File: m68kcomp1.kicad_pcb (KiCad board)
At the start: 2 copper layers, 46 parts, among them P1 CONN_CTL_DATA, P2 CONN_ADDR, P3 POWER, SW1 RST_SW, SW2 PWR_SW, U1 74LS04, U10 sram_um61512ak, U11 sram_um61512ak, U12 68010D, U13 at28c64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

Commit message: laying out the board
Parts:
- U13, U9: footprint Housings_DIP:DIP-28_W15.24mm -> m68kcomp1:DIP-28_W15.24mm_oval
- moved U12 94.0 mm to (160.0, 57.1), turned to 270 degrees
- moved U13 71.9 mm to (101.6, 101.6)
- moved U9 69.4 mm to (81.3, 101.6)
- moved U5 20.3 mm to (91.4, 25.4), turned to 270 degrees
- moved U15 15.2 mm to (160.0, 116.8)
- moved U16 15.2 mm to (176.5, 116.8)
- moved U10 15.2 mm to (127.0, 116.8)
- moved P1 15.2 mm to (199.4, 139.7)
- moved U11 15.2 mm to (143.5, 116.8)
- moved P2 9.67 mm to (196.8, 52.1)
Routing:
- net /D6: track 100.9 -> 154.1 mm
- net /D5: track 96.3 -> 146.4 mm
- net /D4: track 96.6 -> 143.3 mm
- net /D1: track 126.2 -> 171.4 mm
- net /D2: track 125.4 -> 169.8 mm
- net /D0: track 136.6 -> 178.8 mm
- net /D3: track 91.3 -> 130.6 mm
- net /A1: track 77.9 -> 96.7 mm
- net /A3: track 77.9 -> 96.6 mm
- net /A8: track 77.9 -> 96.6 mm
- net /A7: track 77.9 -> 96.6 mm
- net /A6: track 77.9 -> 96.6 mm
- net /A5: track 77.9 -> 96.6 mm
- net /A4: track 77.9 -> 96.6 mm
- net /A13: track 77.9 -> 96.6 mm
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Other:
- board outline added: 160 x 100 mm

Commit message: laying out the board
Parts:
- P2: footprint Pin_Headers:Pin_Header_Straight_2x13 -> m68kcomp1:Pin_Header_Straight_2x13_oval
- moved Y1 216.2 mm to (153.3, 48.8), turned to 180 degrees
- moved U6 205.6 mm to (154.4, 56.0), turned to 270 degrees
- moved U14 197.3 mm to (186.1, 47.0), turned to 270 degrees
- moved SW1 194.1 mm to (165.1, 47.6)
- moved D1 173.5 mm to (61.0, 49.0), turned to 270 degrees
- moved U7 168.2 mm to (135.2, 53.7)
- moved R8 149.6 mm to (57.0, 48.0), turned to 180 degrees
- moved SW2 121.9 mm to (57.0, 53.3), turned to 270 degrees
- moved U5 115.0 mm to (64.3, 137.2), turned to 0 degrees
- moved P3 47.6 mm to (52.0, 53.3)
- moved U12 21.3 mm to (180.3, 63.5)
- moved P2 3.81 mm to (196.8, 55.9)
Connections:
- P2 pad 1: GND -> /A1
- P2 pad 2: /A1 -> GND
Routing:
- net /A4: track 96.6 -> 204.1 mm
- net /A6: track 96.6 -> 203.1 mm
- net /A5: track 96.6 -> 203.1 mm
- net /~WR: track 52.7 -> 158.1 mm, vias 0 -> 1
- net /A2: track 96.5 -> 198.9 mm
- net /A3: track 96.6 -> 198.4 mm
- net /A7: track 96.6 -> 197.0 mm
- net /A8: track 96.6 -> 197.0 mm
- net /A1: track 96.7 -> 193.4 mm
- net /A9: track 89.2 -> 183.5 mm
- net /A10: track 89.2 -> 183.5 mm
- net /A12: track 89.2 -> 177.3 mm
- net /A11: track 89.2 -> 177.3 mm
- net /D0: track 178.8 -> 262.9 mm, vias 0 -> 2
- net /A13: track 96.6 -> 178.6 mm
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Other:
- net class Default: clearance 0.35 -> 0.34
- rule trace_clearance: 0.35 -> 0.34

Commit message: holy shit laying out this PCB takes a lot of time
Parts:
- added C16: 0.1uF, Capacitors_ThroughHole:C_Disc_D7.5_P5, F.Cu at (65.4, 102.8)
- added C17: 0.1uF, Capacitors_ThroughHole:C_Disc_D7.5_P5, F.Cu at (52.1, 102.8)
- C6, R3: moved to B.Cu
- moved C4 229.7 mm to (154.2, 52.2), turned to 270 degrees
- moved C1 216.6 mm to (125.6, 52.3), turned to 90 degrees
- moved R1 208.4 mm to (156.9, 53.5), turned to 90 degrees
- moved C5 205.3 mm to (142.1, 52.4), turned to 270 degrees
- moved R2 189.1 mm to (154.2, 56.1), turned to 270 degrees
- moved C7 184.7 mm to (142.0, 89.3)
- moved R3 181.5 mm to (148.8, 67.1)
- moved R7 180.4 mm to (103.9, 48.5), turned to 90 degrees
- moved C6 177.5 mm to (138.7, 67.1), turned to 180 degrees
- moved R4 176.5 mm to (111.0, 45.1)
- moved U4 171.1 mm to (131.6, 57.1), turned to 90 degrees
- moved U1 161.2 mm to (96.0, 55.8), turned to 180 degrees
- moved C9 156.3 mm to (121.8, 58.7)
- moved C8 150.1 mm to (103.9, 54.5), turned to 90 degrees
- moved U8 135.8 mm to (78.0, 71.5), turned to 90 degrees
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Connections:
- U1 pad 12: (no net) -> /~VPA
- U1 pad 13: GND -> Net-(U1-Pad13)
- U12 pad 21: Net-(U12-Pad21) -> /~VPA
- U2 pad 6: Net-(U2-Pad6) -> Net-(U1-Pad13)
- U6 pad 5: Net-(U2-Pad6) -> GND
- U6 pad 6: Net-(U12-Pad21) -> (no net)
- U7 pad 10: GND -> VCC
- U7 pad 11: GND -> /CLK10
- U7 pad 12: GND -> Net-(U7-Pad12)
- U7 pad 13: GND -> VCC
- U7 pad 8: (no net) -> Net-(U7-Pad12)
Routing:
- net GND: track 40.5 -> 593.0 mm, vias 0 -> 2
- net ~IRQ1: track 0.00 -> 202.2 mm, vias 0 -> 1
- net ~IRQ2: track 0.00 -> 200.7 mm, vias 0 -> 1
- net ~IRQ3: track 0.00 -> 189.9 mm, vias 0 -> 1
- net ~IRQ4: track 0.00 -> 183.8 mm, vias 0 -> 1
- net ~IRQ6: track 0.00 -> 182.7 mm, vias 0 -> 1
- net ~IRQ5: track 0.00 -> 180.0 mm, vias 0 -> 1
- net ~IRQ7: track 0.00 -> 178.8 mm, vias 0 -> 1
- net /CLK20: track 0.00 -> 174.9 mm, vias 0 -> 1
- net ~DTACK: track 0.00 -> 153.2 mm, vias 0 -> 1
- net VCC: track 6.91 -> 158.3 mm
- net /A23: track 48.8 -> 158.7 mm, vias 0 -> 2
- net /A22: track 54.9 -> 160.6 mm, vias 0 -> 2
- net /A17: track 103.8 -> 207.2 mm, vias 0 -> 3
- net /A21: track 54.9 -> 156.0 mm, vias 0 -> 2
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
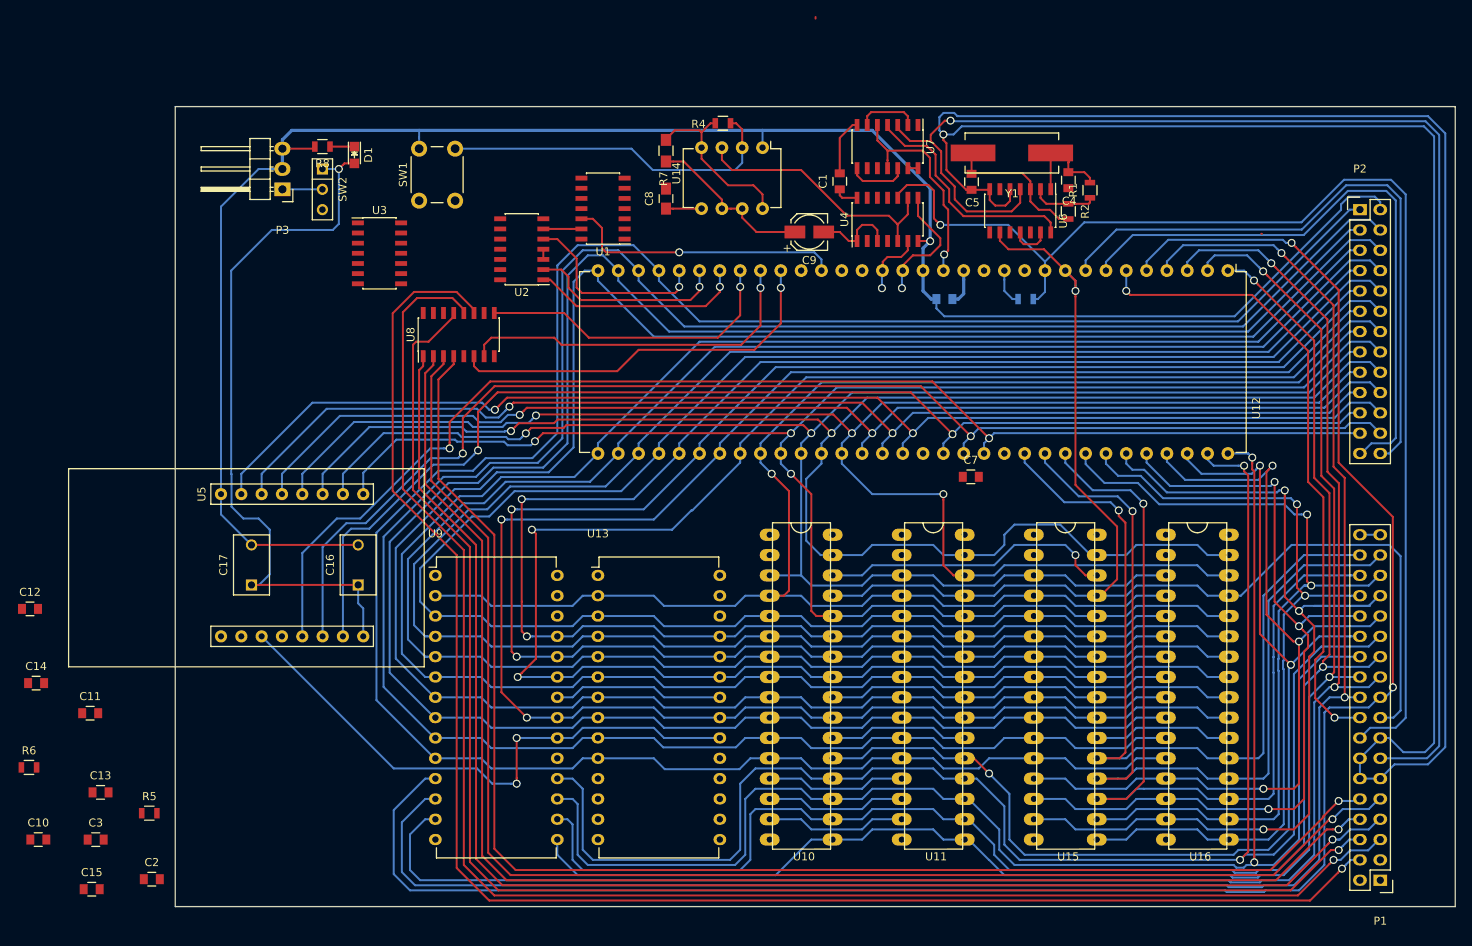
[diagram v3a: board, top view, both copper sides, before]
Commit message: pcb layout almost done
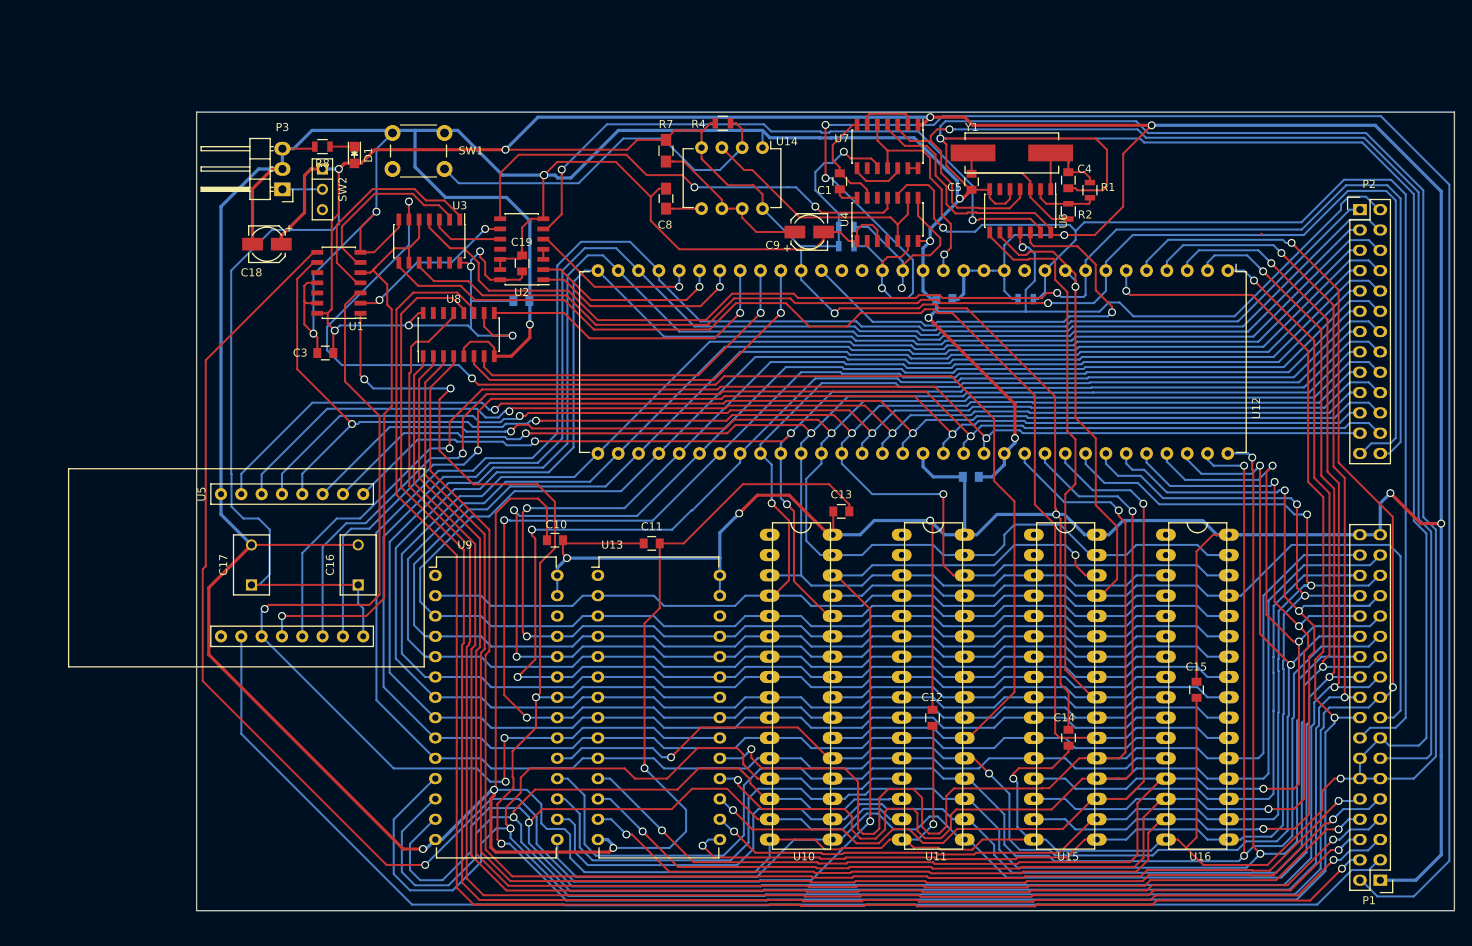
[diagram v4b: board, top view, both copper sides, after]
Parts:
- added C18: 4.7uF, Capacitors_SMD:c_elec_4x5.7, F.Cu at (54.0, 60.2)
- added C19: 0.1uF, Capacitors_SMD:C_0805, F.Cu at (85.9, 62.6)
- C2, C7, R5, R6: moved to B.Cu
- moved C15 140.3 mm to (170.2, 115.9), turned to 270 degrees
- moved C14 129.2 mm to (154.2, 121.9), turned to 270 degrees
- moved R6 121.2 mm to (126.4, 60.5), turned to 180 degrees
- moved R5 113.8 mm to (126.4, 58.0)
- moved C12 113.6 mm to (137.2, 119.4), turned to 270 degrees
- moved C13 99.0 mm to (125.8, 93.6)
- moved C2 85.8 mm to (85.8, 67.3)
- moved C10 74.6 mm to (90.0, 97.2), turned to 180 degrees
- moved C11 73.3 mm to (102.1, 97.6)
- moved C3 67.3 mm to (61.3, 73.8), turned to 180 degrees
- moved U1 34.3 mm to (63.0, 65.0)
- moved SW1 9.09 mm to (69.7, 46.3), turned to 0 degrees
- moved U3 6.41 mm to (74.3, 59.8), turned to 270 degrees
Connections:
- U1 pad 12: /~VPA -> (no net)
- U1 pad 13: Net-(U1-Pad13) -> GND
- U2 pad 6: Net-(U1-Pad13) -> Net-(U2-Pad6)
- U6 pad 12: (no net) -> /~VPA
- U6 pad 13: GND -> Net-(U2-Pad6)
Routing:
- net VCC: track 158.3 -> 875.9 mm, vias 1 -> 18
- net GND: track 593.0 -> 1234.8 mm, vias 2 -> 18
- net /~AS: track 101.0 -> 321.9 mm, vias 2 -> 6
- net ~SYS_RESET: track 9.00 -> 225.4 mm, vias 1 -> 3
- net Net-(U1-Pad8): track 36.9 -> 235.5 mm, vias 1 -> 3
- net /~IOEN: track 0.00 -> 165.8 mm
- net Net-(U10-Pad22): track 17.6 -> 174.3 mm, vias 0 -> 2
- net Net-(U15-Pad22): track 17.6 -> 157.4 mm
- net ~LDS: track 78.8 -> 173.4 mm, vias 0 -> 1
- net ~UDS: track 76.5 -> 170.9 mm, vias 0 -> 1
- net /D8: track 104.5 -> 188.3 mm, vias 3 -> 4
- net /D9: track 104.2 -> 185.5 mm, vias 3 -> 4
- net Net-(U2-Pad6): track 0.00 -> 79.5 mm, vias 0 -> 2
- net /D10: track 119.7 -> 198.5 mm, vias 3 -> 4
- net /~RAMEN: track 0.00 -> 72.4 mm, vias 0 -> 1
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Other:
- board size 160 x 100 mm -> 157.2 x 99.8 mm

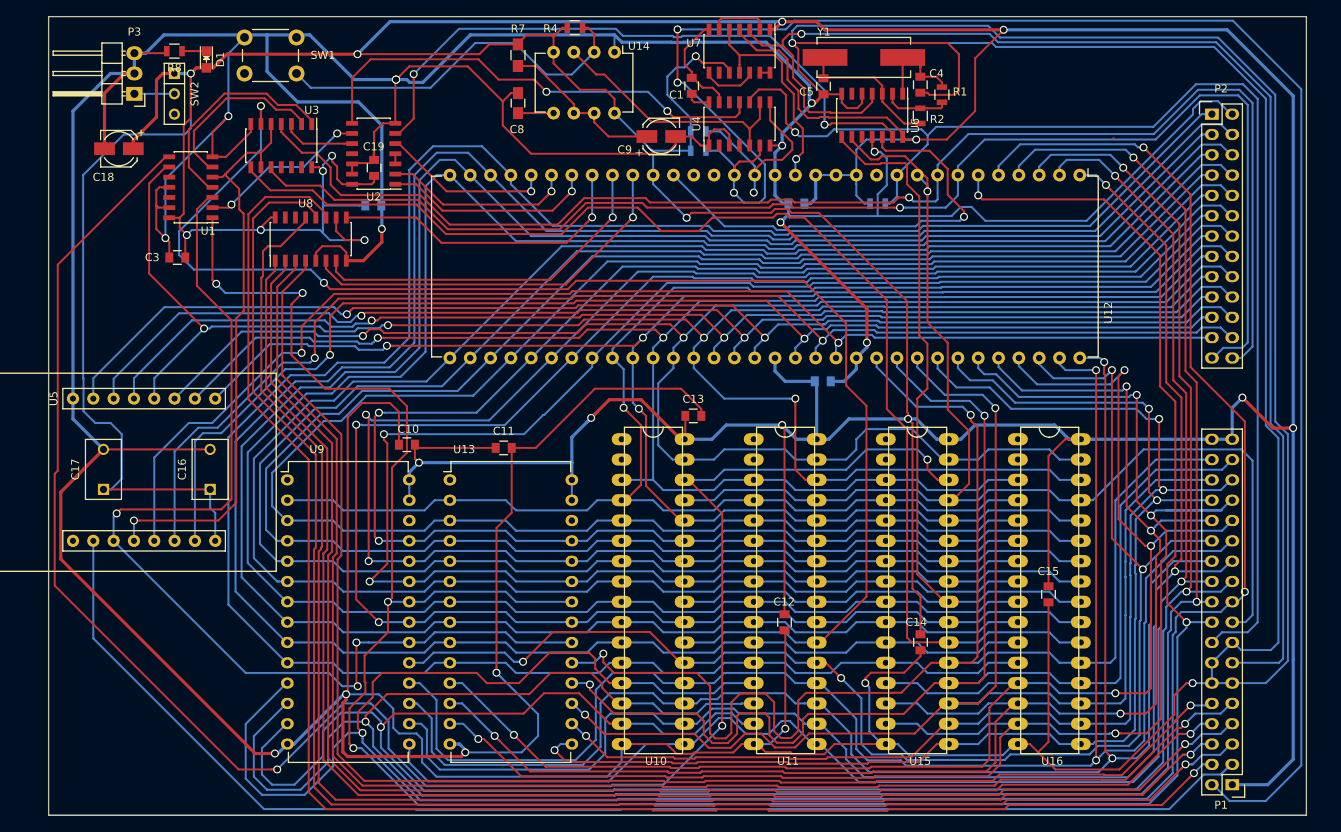
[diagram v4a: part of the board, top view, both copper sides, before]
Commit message: completed pcb layout
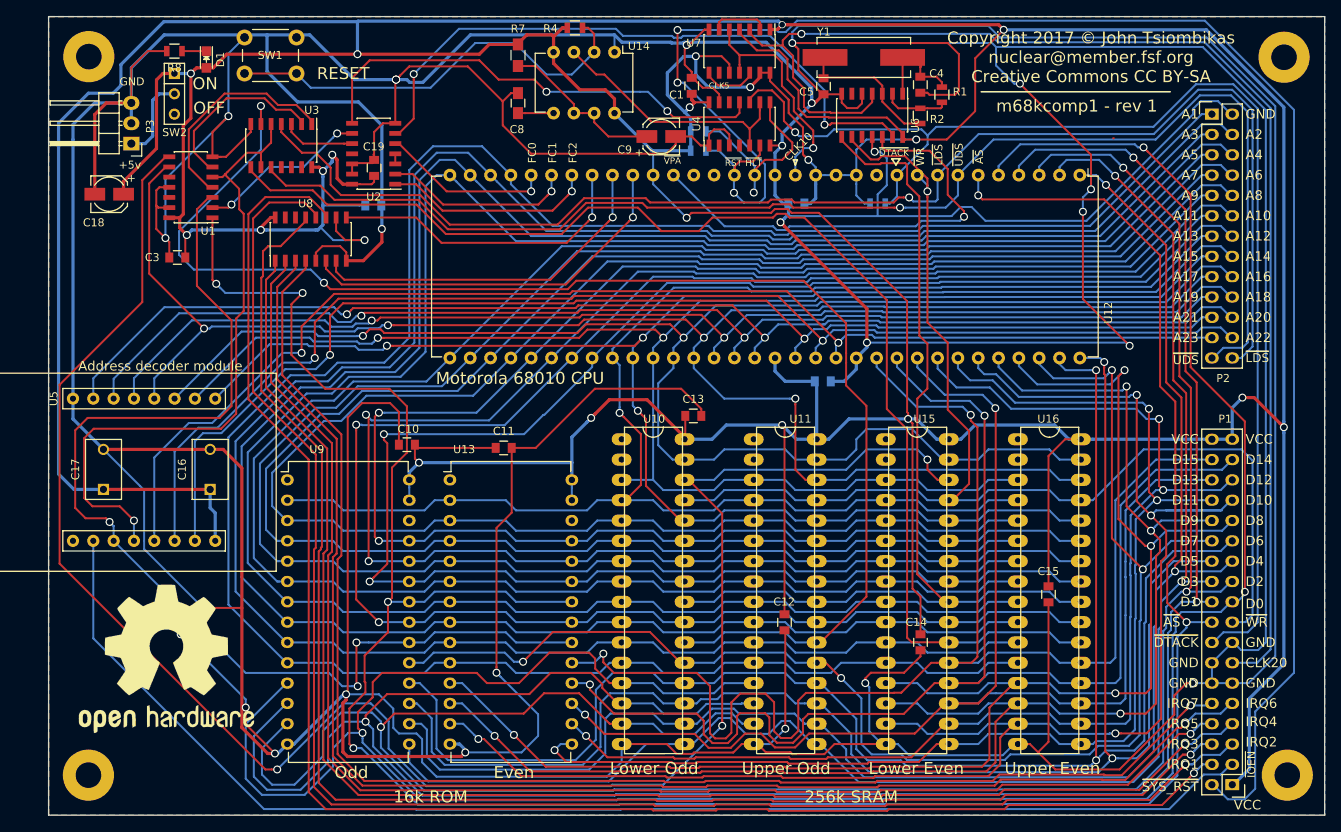
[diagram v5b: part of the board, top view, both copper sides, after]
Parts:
- added REF**: MountingHole_3.2mm_M3_Pad, Mounting_Holes:MountingHole_3.2mm_M3_Pad, F.Cu at (50.2, 48.7)
- added REF**: MountingHole_3.2mm_M3_Pad, Mounting_Holes:MountingHole_3.2mm_M3_Pad, F.Cu at (50.2, 138.5)
- added REF**: MountingHole_3.2mm_M3_Pad, Mounting_Holes:MountingHole_3.2mm_M3_Pad, F.Cu at (199.6, 48.8)
- added REF**: MountingHole_3.2mm_M3_Pad, Mounting_Holes:MountingHole_3.2mm_M3_Pad, F.Cu at (200.1, 138.5)
- added REF***: OSHW-Logo2_24.3x20mm_SilkScreen, Symbols:OSHW-Logo2_24.3x20mm_SilkScreen, F.Cu at (59.9, 124.0)
- moved P3 6.23 mm to (55.6, 59.6)
- moved C18 5.82 mm to (52.8, 65.9)
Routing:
- net GND: track 1234.8 -> 1363.6 mm, vias 18 -> 26
- net VCC: track 875.9 -> 935.6 mm, vias 18 -> 21
- net /~RAMEN: track 72.4 -> 82.7 mm
- net /~ROMEN: track 130.8 -> 138.6 mm
- net Net-(R4-Pad2): track 47.1 -> 53.6 mm
- net /5v: track 5.00 -> 10.6 mm
- net ~SYS_RESET: track 225.4 -> 221.0 mm
- net /CLK20: track 167.1 -> 163.4 mm
- net Net-(U1-Pad8): track 235.5 -> 233.0 mm
- net /CLK10: track 27.2 -> 28.9 mm
- net ~DTACK: track 156.2 -> 154.7 mm
- net ~LDS: track 173.4 -> 172.1 mm
- net ~UDS: track 170.9 -> 169.8 mm
- added copper zone on B.Cu, net GND
- added copper zone on F.Cu, net GND
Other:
- board size 157.2 x 99.8 mm -> 159.5 x 99.8 mm
- net class Default: clearance 0.34 -> 0.25
- rule trace_clearance: 0.34 -> 0.25
- board text added: "+5v"
- board text added: "16k ROM"
- board text added: "256k SRAM"
- board text added: "A1"
- board text added: "A10"
- board text added: "A11"
- board text added: "A12"
- board text added: "A13"
- board text added: "A14"
- board text added: "A15"
- board text added: "A16"
- board text added: "A17"
- board text added: "A18"
- board text added: "A19"
- board text added: "A2"
- board text added: "A20"
- board text added: "A21"
- board text added: "A22"
- board text added: "A23"
- board text added: "A3"
- board text added: "A4"
- board text added: "A5"
- board text added: "A6"
- board text added: "A7"
- board text added: "A8"
- board text added: "A9"
- board text added: "Address decoder module"
- board text added: "CLK10"
- board text added: "CLK20"
- board text added: "CLK5"
- board text added: "Copyright 2017 © John Tsiombikas nuclear@member.fsf.org Creative Commons CC BY-SA"
- board text added: "D0"
- board text added: "D1"
- board text added: "D10"
- board text added: "D11"
- board text added: "D12"
- board text added: "D13"
- board text added: "D14"
- board text added: "D15"
- board text added: "D2"
- board text added: "D3"
- board text added: "D4"
- board text added: "D5"
- board text added: "D6"
- board text added: "D7"
- board text added: "D8"
- board text added: "D9"
- board text added: "Even"
- board text added: "FC0"
- board text added: "FC1"
- board text added: "FC2"
- board text added: "GND"
- board text added: "IRQ1"
- board text added: "IRQ2"
- board text added: "IRQ3"
- board text added: "IRQ4"
- board text added: "IRQ5"
- board text added: "IRQ6"
- board text added: "IRQ7"
- board text added: "Lower Even"
- board text added: "Lower Odd"
- board text added: "Motorola 68010 CPU"
- board text added: "OFF"
- board text added: "ON"
- board text added: "Odd"
- board text added: "RESET"
- board text added: "Upper Even"
- board text added: "Upper Odd"
- board text added: "VCC"
- board text added: "m68kcomp1 - rev 1"
- board text added: "~AS"
- board text added: "~DTACK"
- board text added: "~HLT"
- board text added: "~IOEN"
- board text added: "~LDS"
- board text added: "~RST"
- board text added: "~SYS_RST"
- board text added: "~UDS"
- board text added: "~VPA"
- board text added: "~WR"

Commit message: changes for manufacture
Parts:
- P1: footprint m68kcomp1:Pin_Header_Straight_2x18 -> Pin_Header_Straight_2x18
- P2: footprint m68kcomp1:Pin_Header_Straight_2x13_oval -> Pin_Header_Straight_2x13_oval
